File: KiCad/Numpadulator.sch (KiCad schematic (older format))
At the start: 61 parts, among them SW1 Cherry_MX_RGB_WS2812, SW10 Cherry_MX_RGB_WS2812, SW11 Cherry_MX_RGB_WS2812, SW12 Cherry_MX_RGB_WS2812, SW13 Cherry_MX_RGB_WS2812, SW14 Cherry_MX_RGB_WS2812, SW15 Cherry_MX_RGB_WS2812, SW16 Cherry_MX_RGB_WS2812, SW19 Rotary_Encoder_Switch, SW2 Cherry_MX_RGB_WS2812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

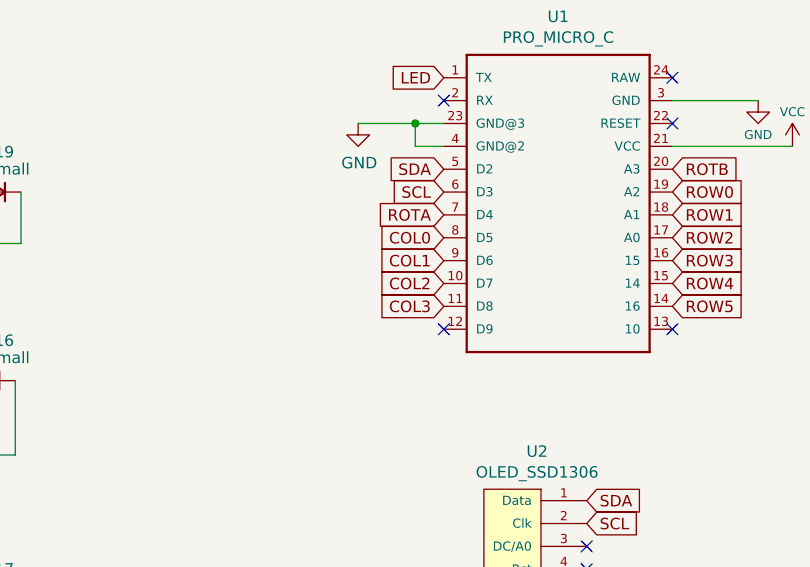
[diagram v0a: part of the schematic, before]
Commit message: added some whack wiring for LEDs and some Columns
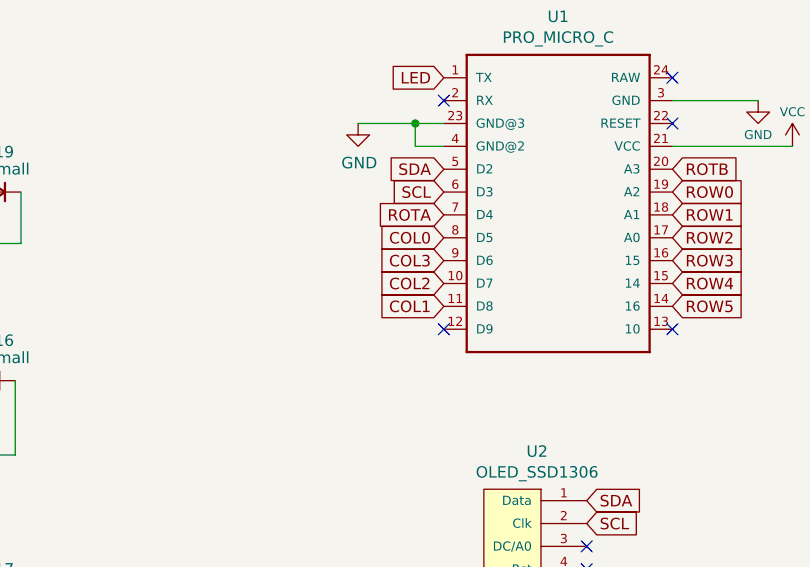
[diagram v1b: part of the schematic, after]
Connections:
- net COL1: now also U1.11 (D8); no longer U1.9 (D6)
- net COL3: now also U1.9 (D6); no longer U1.11 (D8)
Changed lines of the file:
@@
 COL2
 Text GLabel 9200 1675 0    50   Input ~ 0
-COL1
+COL3
 Text GLabel 9200 1575 0    50   Input ~ 0
 COL0
@@
 SDA
 Text GLabel 9200 1875 0    50   Input ~ 0
-COL3
+COL1
 Text GLabel 9200 1475 0    50   Input ~ 0
 ROTA

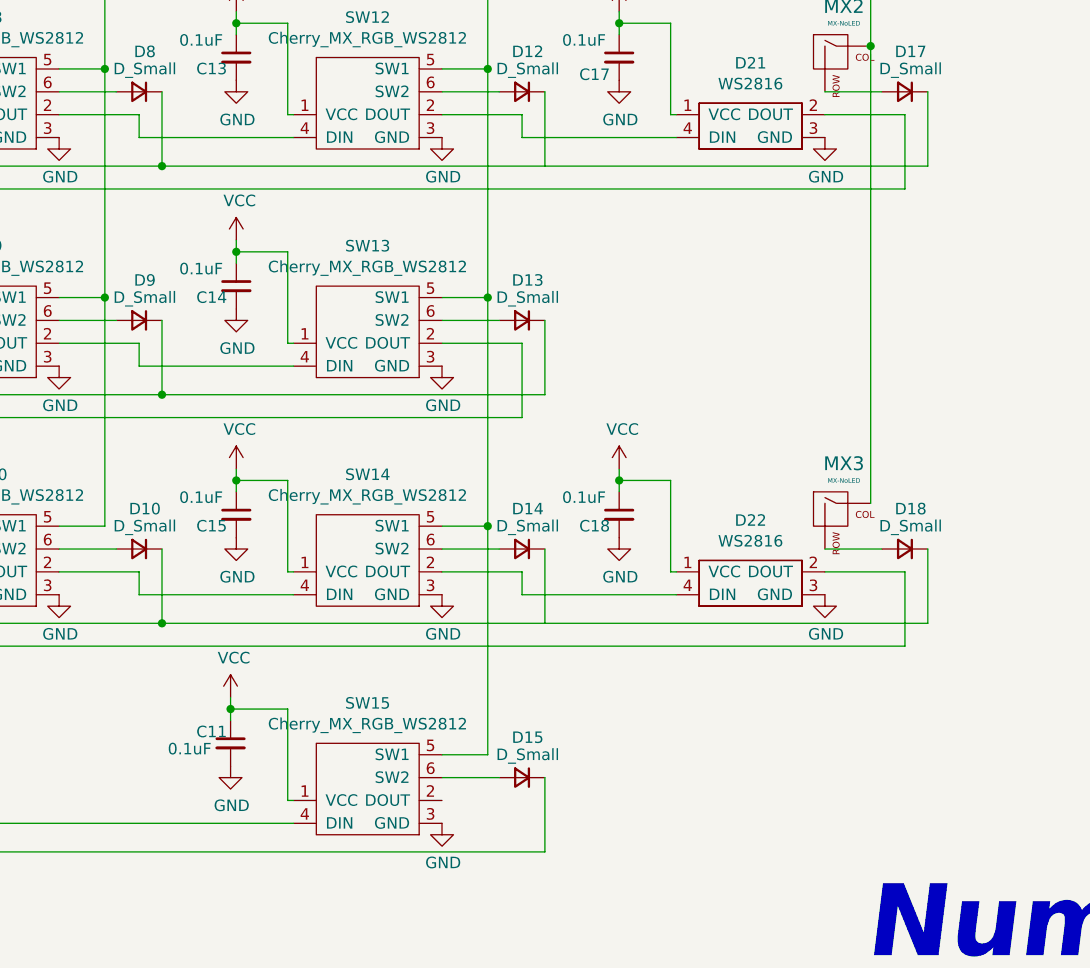
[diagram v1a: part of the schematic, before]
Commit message: Wired up rows, realized there is something wrong with the 2u keys rows in the schematic...
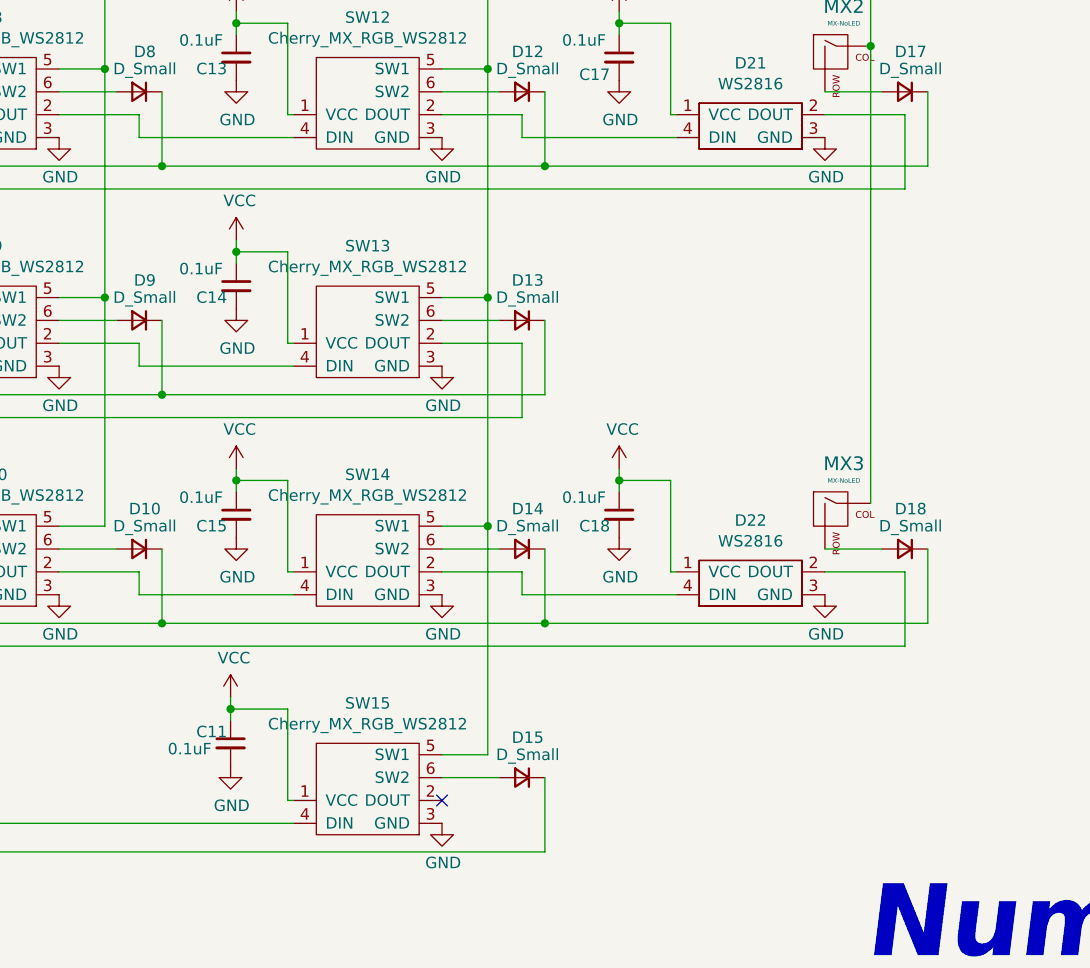
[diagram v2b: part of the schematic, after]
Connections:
- net ROW2: now also D12.1 (K)
- net ROW4: now also D14.1 (K)
- no-connect marks 9 -> 10
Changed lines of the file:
@@
 Wire Wire Line
 	3875 3400 4550 3400
-Wire Wire Line
-	5650 3200 5650 3525
 $Comp
 L Numpadulator-rescue:D_Small-Device D12
@@
 $EndComp
 Wire Wire Line
-	3975 3525 7325 3525
+	3975 3525 5650 3525
 Connection ~ 3725 2100
 Wire Wire Line
@@
 Wire Wire Line
 	3875 5400 4550 5400
-Wire Wire Line
-	5650 5200 5650 5525
 $Comp
 L Numpadulator-rescue:D_Small-Device D14
@@
 $EndComp
 Wire Wire Line
-	3975 5525 7325 5525
-Wire Wire Line
 	1075 4625 1075 5400
 $Comp
@@
 Wire Wire Line
 	1850 6300 2200 6300
+Wire Wire Line
+	5650 3200 5650 3525
+Connection ~ 5650 3525
+Wire Wire Line
+	5650 3525 7325 3525
+Wire Wire Line
+	3975 5525 5650 5525
+Wire Wire Line
+	5650 5200 5650 5525
+Connection ~ 5650 5525
+Wire Wire Line
+	5650 5525 7325 5525
+NoConn ~ 5200 6300
 $EndSCHEMATC

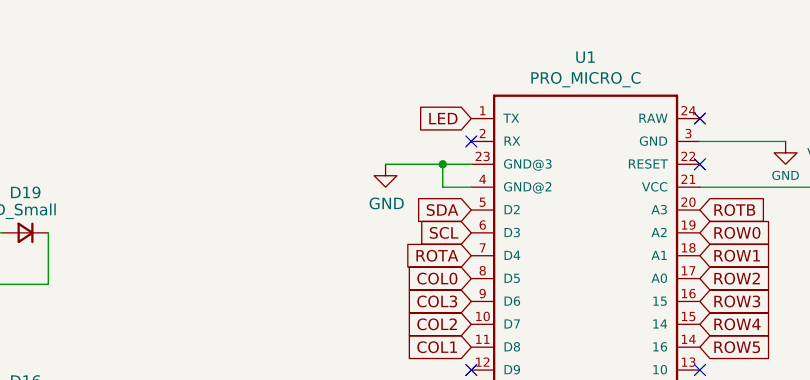
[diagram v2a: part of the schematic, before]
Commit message: add resistor coming from LED pin
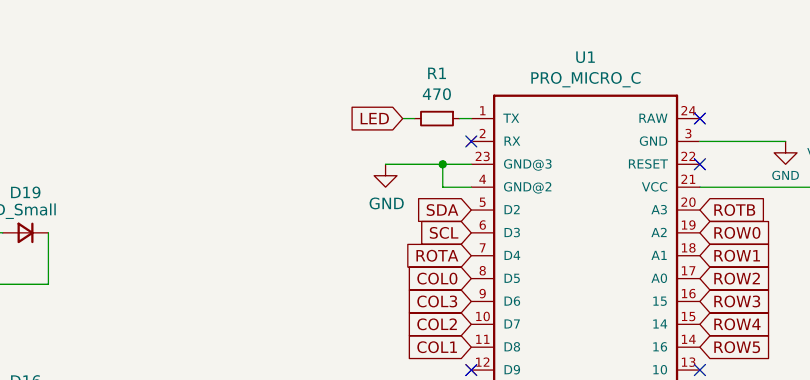
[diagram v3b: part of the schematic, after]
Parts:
- added R1: 470, Resistor_SMD:R_0805_2012Metric, symbol Device:R_Small
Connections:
- net LED: now also R1.2; no longer U1.1 (TX)
- new net: R1.1, U1.1 (TX)
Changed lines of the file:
@@
 Text GLabel 10200 1375 2    50   Input ~ 0
 ROW0
-Text GLabel 9200 875  0    50   Input ~ 0
+Text GLabel 8900 875  0    50   Input ~ 0
 LED
 $Comp
@@
 	5650 5525 7325 5525
 NoConn ~ 5200 6300
+$Comp
+L Device:R_Small R1
+U 1 1 602D0601
+P 9050 875
+F 0 "R1" V 8854 875 50  0000 C CNN
+F 1 "470" V 8945 875 50  0000 C CNN
+F 2 "Resistor_SMD:R_0805_2012Metric" H 9050 875 50  0001 C CNN
+F 3 "~" H 9050 875 50  0001 C CNN
+	1    9050 875
+	0    1    1    0
+$EndComp
+Wire Wire Line
+	9200 875  9150 875
+Wire Wire Line
+	8950 875  8900 875
 $EndSCHEMATC

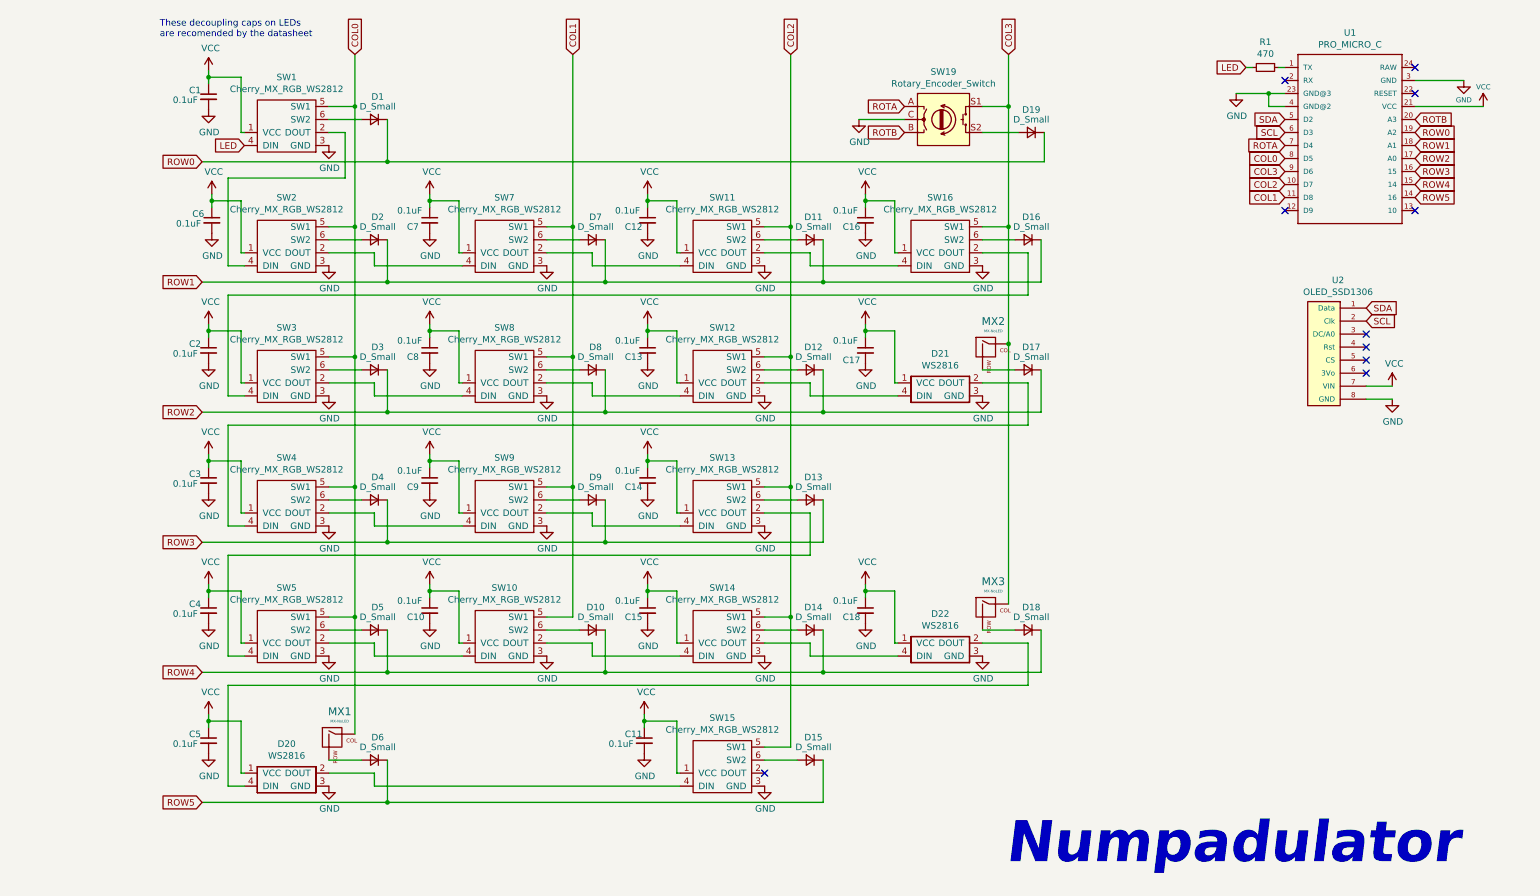
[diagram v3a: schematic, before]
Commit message: got underglow LEDs in schematic... gotta wire them up now
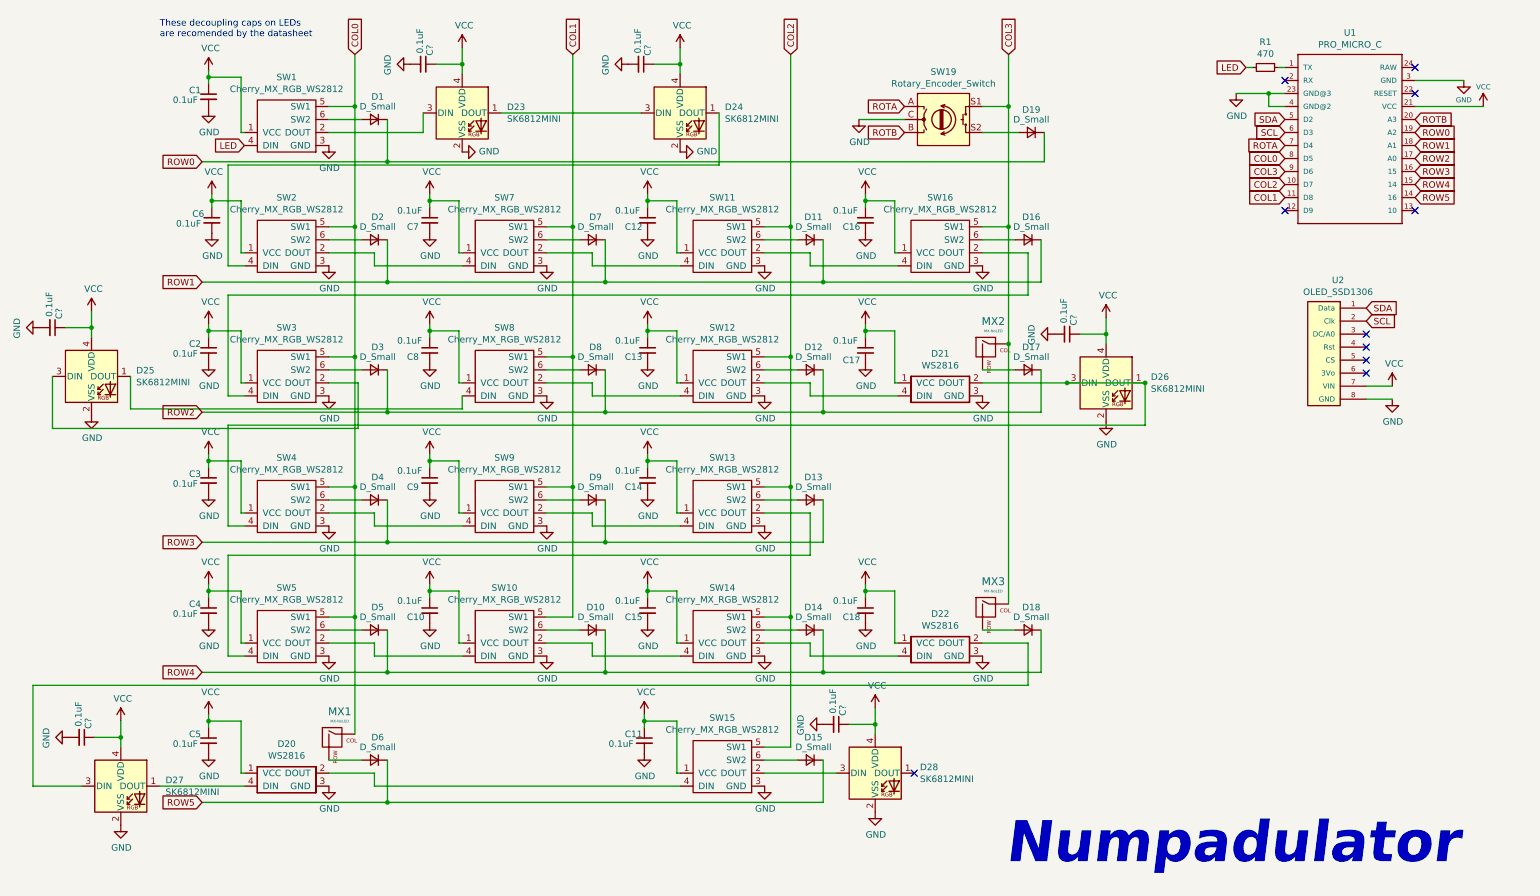
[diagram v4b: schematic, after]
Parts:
- added C? (x6): 0.1uF, Capacitor_SMD:C_0805_2012Metric, symbol Numpadulator-rescue:C_Small-Device
- added D23, D24, D25, D26, D27, D28: SK6812MINI, LED_SMD:LED_SK6812MINI_PLCC4_3.5x3.5mm_P1.75mm, symbol LED:SK6812MINI
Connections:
- net GND: now also C?.2, C?.2, C?.2, C?.2, C?.2, C?.2, D23.2 (VSS), D24.2 (VSS), D25.2 (VSS), D26.2 (VSS), D27.2 (VSS), D28.2 (VSS)
- net VCC: now also C?.1, C?.1, C?.1, C?.1, C?.1, C?.1, D23.4 (VDD), D24.4 (VDD), D25.4 (VDD), D26.4 (VDD), D27.4 (VDD), D28.4 (VDD)
- net at SW1.2 (DOUT): now also D23.3 (DIN); no longer SW2.4 (DIN)
- net at D21.2 (DOUT), SW4.4 (DIN): now also D26.1 (DOUT), D26.3 (DIN)
- net at SW8.4 (DIN): now also D25.1 (DOUT); no longer SW3.2 (DOUT)
- net at D22.2 (DOUT): now also D27.3 (DIN); no longer D20.4 (DIN)
- net at SW15.2 (DOUT): now also D28.3 (DIN)
- new net: D24.1 (DOUT), SW2.4 (DIN)
- new net: D25.3 (DIN), SW3.2 (DOUT)
- new net: D20.4 (DIN), D27.1 (DOUT)
- new net: D23.1 (DOUT), D24.3 (DIN)
